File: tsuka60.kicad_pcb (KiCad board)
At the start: 2 copper layers, 285 x 95.1 mm, 175 parts, among them SW1 SW_Push, U1 ATmega32U4-AU, Y1 Resonator_Small

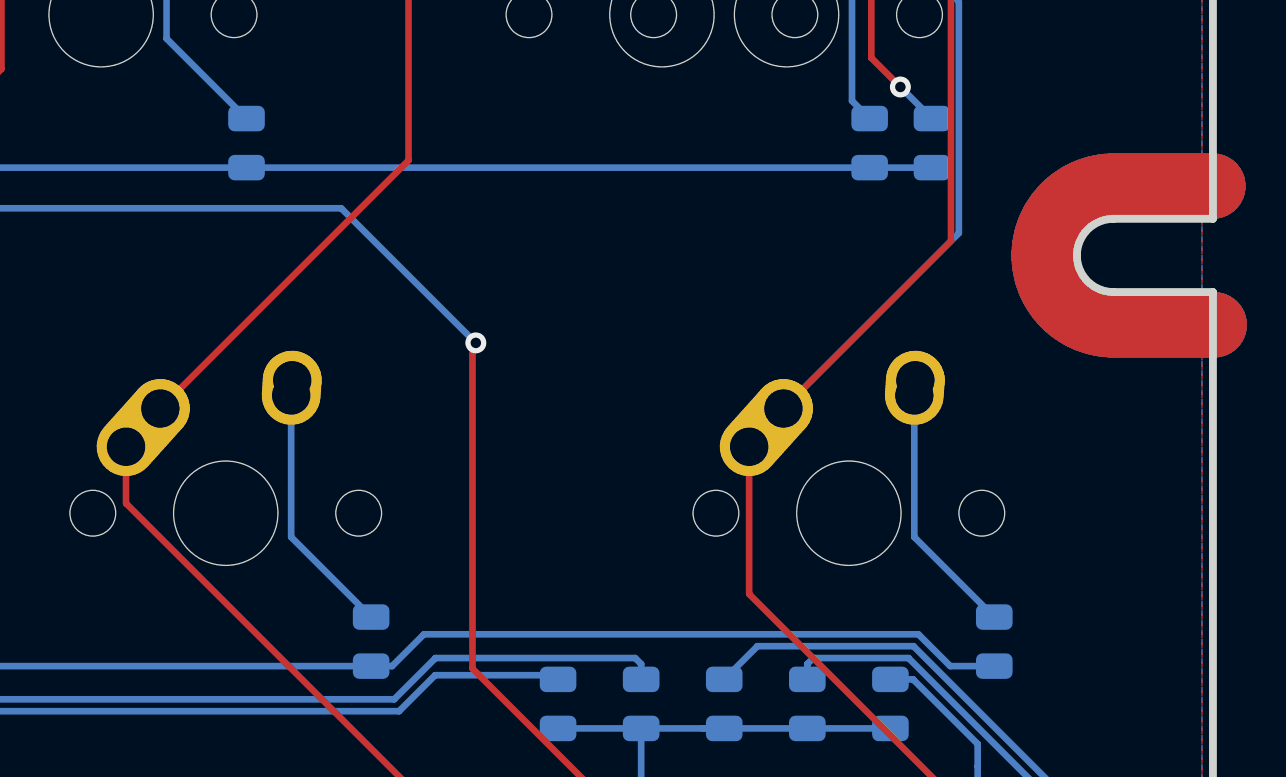
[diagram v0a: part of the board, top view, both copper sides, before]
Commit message: Added alternative right-shift keys
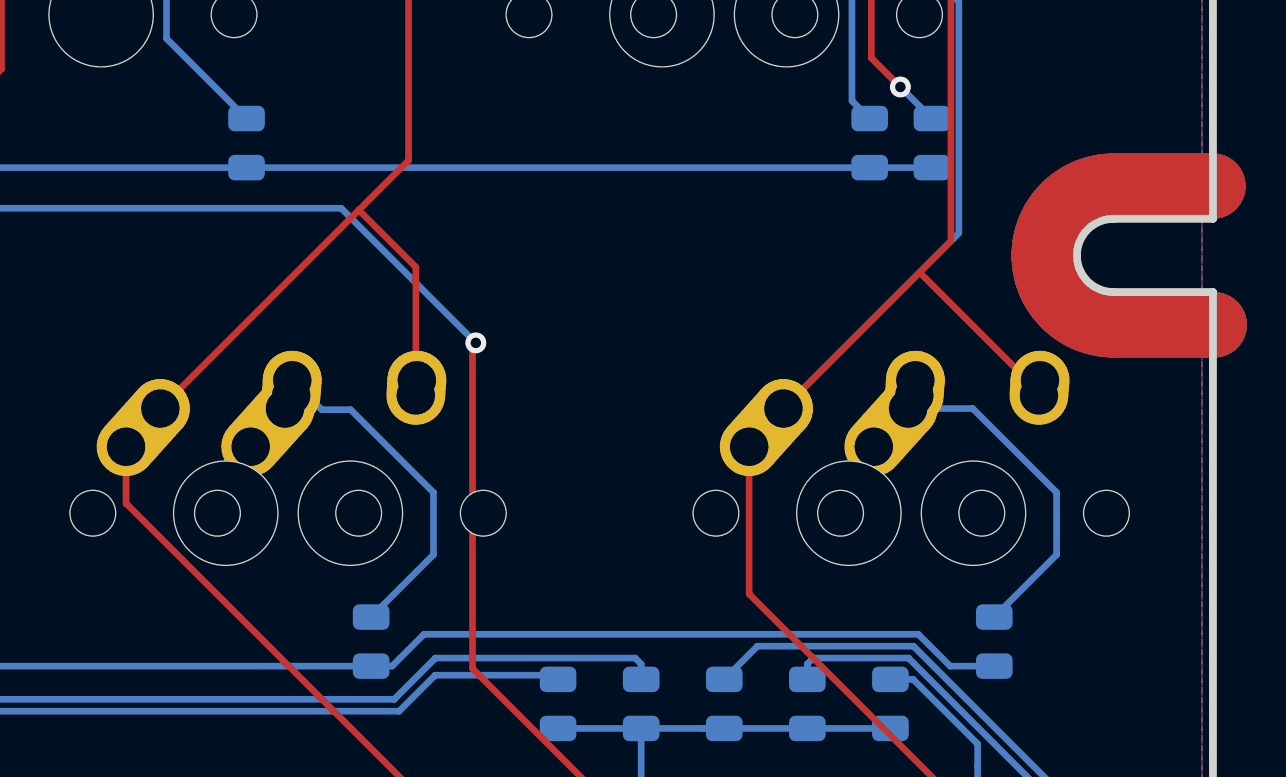
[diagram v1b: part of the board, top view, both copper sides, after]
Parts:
- added MX59-1: SLASH, MX_Alps_Hybrid:MX-1.5U-NoLED, F.Cu at (346.9, 178.6)
- added MX60-1: R-SHIFT, MX_Alps_Hybrid:MX-1U-NoLED, F.Cu at (370.7, 178.6)
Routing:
- net Col13: track 361.5 -> 369.5 mm
- net Col14: track 385.4 -> 392.0 mm
- net Net-(D59-Pad2): track 9.73 -> 12.9 mm
- net Net-(D60-Pad2): track 9.73 -> 12.8 mm
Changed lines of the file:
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@@
     (thickness 1.6)
     (drawings 1)
-    (tracks 1058)
+    (tracks 1069)
     (zones 0)
-    (modules 175)
+    (modules 177)
     (nets 114)
   )
@@
     (38 B.Mask user hide)
     (39 F.Mask user hide)
-    (40 Dwgs.User user hide)
+    (40 Dwgs.User user)
     (41 Cmts.User user hide)
     (42 Eco1.User user hide)
@@
     )
   )
+  (module MX_Alps_Hybrid:MX-1.5U-NoLED (layer F.Cu)
+    (at 346.86875 178.59375)
+    (fp_text reference MX59-1 (at 0 3.175) (layer Dwgs.User)
+      (effects (font (size 1 1) (thickness 0.15)))
+    )
+    (fp_text value SLASH (at 0 -7.9375) (layer Dwgs.User)
+      (effects (font (size 1 1) (thickness 0.15)))
+    )
+    (fp_line (start 5 -7) (end 7 -7) (layer Dwgs.User) (width 0.15))
+    (fp_line (start 7 -7) (end 7 -5) (layer Dwgs.User) (width 0.15))
+    (fp_line (start 5 7) (end 7 7) (layer Dwgs.User) (width 0.15))
+    (fp_line (start 7 7) (end 7 5) (layer Dwgs.User) (width 0.15))
+    (fp_line (start -7 5) (end -7 7) (layer Dwgs.User) (width 0.15))
+    (fp_line (start -7 7) (end -5 7) (layer Dwgs.User) (width 0.15))
+    (fp_line (start -5 -7) (end -7 -7) (layer Dwgs.User) (width 0.15))
+    (fp_line (start -7 -7) (end -7 -5) (layer Dwgs.User) (width 0.15))
+    (fp_line (start -14.2875 -9.525) (end 14.2875 -9.525) (layer Dwgs.User) (width 0.15))
+    (fp_line (start 14.2875 -9.525) (end 14.2875 9.525) (layer Dwgs.User) (width 0.15))
+    (fp_line (start 14.2875 9.525) (end -14.2875 9.525) (layer Dwgs.User) (width 0.15))
+    (fp_line (start -14.2875 9.525) (end -14.2875 -9.525) (layer Dwgs.User) (width 0.15))
+    (pad 2 thru_hole oval (at 2.5 -4.5 86.0548) (size 2.831378 2.25) (drill 1.47 (offset 0.290689 0)) (layers *.Cu B.Mask)
+      (net 92 Col13))
+    (pad 2 thru_hole circle (at 2.54 -5.08) (size 2.25 2.25) (drill 1.47) (layers *.Cu B.Mask)
+      (net 92 Col13))
+    (pad 1 thru_hole oval (at -3.81 -2.54 48.0996) (size 4.211556 2.25) (drill 1.47 (offset 0.980778 0)) (layers *.Cu B.Mask)
+      (net 62 "Net-(D59-Pad2)"))
+    (pad "" np_thru_hole circle (at 0 0) (size 3.9878 3.9878) (drill 3.9878) (layers *.Cu *.Mask))
+    (pad 1 thru_hole circle (at -2.5 -4) (size 2.25 2.25) (drill 1.47) (layers *.Cu B.Mask)
+      (net 62 "Net-(D59-Pad2)"))
+    (pad "" np_thru_hole circle (at -5.08 0 48.0996) (size 1.75 1.75) (drill 1.75) (layers *.Cu *.Mask))
+    (pad "" np_thru_hole circle (at 5.08 0 48.0996) (size 1.75 1.75) (drill 1.75) (layers *.Cu *.Mask))
+  )
+  (module MX_Alps_Hybrid:MX-1U-NoLED (layer F.Cu)
+    (at 370.68125 178.59375)
+    (fp_text reference MX60-1 (at 0 3.175) (layer Dwgs.User)
+      (effects (font (size 1 1) (thickness 0.15)))
+    )
+    (fp_text value R-SHIFT (at 0 -7.9375) (layer Dwgs.User)
+      (effects (font (size 1 1) (thickness 0.15)))
+    )
+    (fp_line (start 5 -7) (end 7 -7) (layer Dwgs.User) (width 0.15))
+    (fp_line (start 7 -7) (end 7 -5) (layer Dwgs.User) (width 0.15))
+    (fp_line (start 5 7) (end 7 7) (layer Dwgs.User) (width 0.15))
+    (fp_line (start 7 7) (end 7 5) (layer Dwgs.User) (width 0.15))
+    (fp_line (start -7 5) (end -7 7) (layer Dwgs.User) (width 0.15))
+    (fp_line (start -7 7) (end -5 7) (layer Dwgs.User) (width 0.15))
+    (fp_line (start -5 -7) (end -7 -7) (layer Dwgs.User) (width 0.15))
+    (fp_line (start -7 -7) (end -7 -5) (layer Dwgs.User) (width 0.15))
+    (fp_line (start -9.525 -9.525) (end 9.525 -9.525) (layer Dwgs.User) (width 0.15))
+    (fp_line (start 9.525 -9.525) (end 9.525 9.525) (layer Dwgs.User) (width 0.15))
+    (fp_line (start 9.525 9.525) (end -9.525 9.525) (layer Dwgs.User) (width 0.15))
+    (fp_line (start -9.525 9.525) (end -9.525 -9.525) (layer Dwgs.User) (width 0.15))
+    (pad 2 thru_hole oval (at 2.5 -4.5 86.0548) (size 2.831378 2.25) (drill 1.47 (offset 0.290689 0)) (layers *.Cu B.Mask)
+      (net 93 Col14))
+    (pad 2 thru_hole circle (at 2.54 -5.08) (size 2.25 2.25) (drill 1.47) (layers *.Cu B.Mask)
+      (net 93 Col14))
+    (pad 1 thru_hole oval (at -3.81 -2.54 48.0996) (size 4.211556 2.25) (drill 1.47 (offset 0.980778 0)) (layers *.Cu B.Mask)
+      (net 63 "Net-(D60-Pad2)"))
+    (pad "" np_thru_hole circle (at 0 0) (size 3.9878 3.9878) (drill 3.9878) (layers *.Cu *.Mask))
+    (pad 1 thru_hole circle (at -2.5 -4) (size 2.25 2.25) (drill 1.47) (layers *.Cu B.Mask)
+      (net 63 "Net-(D60-Pad2)"))
+    (pad "" np_thru_hole circle (at -5.08 0 48.0996) (size 1.75 1.75) (drill 1.75) (layers *.Cu *.Mask))
+    (pad "" np_thru_hole circle (at 5.08 0 48.0996) (size 1.75 1.75) (drill 1.75) (layers *.Cu *.Mask))
+  )
   (gr_text "Tsuka60 aka Semi Ergo Layout\nPrototype Two\nby RominRonin" (at 127.762 131.064) (layer B.SilkS)
     (effects (font (size 1.016 1.016) (thickness 0.254)) (justify right mirror))
@@
   (segment (start 325.55625 179.50625) (end 328.6125 182.5625) (width 0.254) (layer B.Cu) (net 61))
   (segment (start 325.55625 174.09375) (end 325.55625 179.50625) (width 0.254) (layer B.Cu) (net 61))
-  (segment (start 344.60625 179.50625) (end 347.6625 182.5625) (width 0.254) (layer B.Cu) (net 62))
-  (segment (start 344.60625 174.09375) (end 344.60625 179.50625) (width 0.254) (layer B.Cu) (net 62))
-  (segment (start 368.41875 179.50625) (end 371.475 182.5625) (width 0.254) (layer B.Cu) (net 63))
-  (segment (start 368.41875 174.09375) (end 368.41875 179.50625) (width 0.254) (layer B.Cu) (net 63))
+  (segment (start 347.6625 182.5625) (end 350.04375 180.18125) (width 0.254) (layer B.Cu) (net 62))
+  (segment (start 350.04375 180.18125) (end 350.04375 177.8) (width 0.254) (layer B.Cu) (net 62))
+  (segment (start 345.771249 174.638749) (end 344.64625 173.51375) (width 0.254) (layer B.Cu) (net 62))
+  (segment (start 346.882499 174.638749) (end 345.771249 174.638749) (width 0.254) (layer B.Cu) (net 62))
+  (segment (start 350.04375 177.8) (end 346.882499 174.638749) (width 0.254) (layer B.Cu) (net 62))
+  (segment (start 370.65 174.59375) (end 368.18125 174.59375) (width 0.254) (layer B.Cu) (net 63))
+  (segment (start 373.85625 180.18125) (end 373.85625 177.8) (width 0.254) (layer B.Cu) (net 63))
+  (segment (start 373.85625 177.8) (end 370.65 174.59375) (width 0.254) (layer B.Cu) (net 63))
+  (segment (start 371.475 182.5625) (end 373.85625 180.18125) (width 0.254) (layer B.Cu) (net 63))
   (segment (start 138.9125 203.4875) (end 161.925 203.4875) (width 0.254) (layer B.Cu) (net 64))
   (segment (start 138.1125 203.4875) (end 138.9125 203.4875) (width 0.254) (layer B.Cu) (net 64))
@@
   (segment (start 349.09125 144.812712) (end 358.742288 154.46375) (width 0.254) (layer F.Cu) (net 92))
   (segment (start 349.09125 144.30375) (end 349.09125 144.812712) (width 0.254) (layer F.Cu) (net 92))
-  (segment (start 349.09125 165.10875) (end 339.60625 174.59375) (width 0.254) (layer F.Cu) (net 92))
-  (segment (start 349.09125 144.30375) (end 349.09125 165.10875) (width 0.254) (layer F.Cu) (net 92))
   (segment (start 347.82125 118.90375) (end 347.82125 123.22175) (width 0.254) (layer F.Cu) (net 92))
   (segment (start 345.099249 140.311749) (end 349.09125 144.30375) (width 0.254) (layer F.Cu) (net 92))
@@
   (segment (start 156.462518 147.90101) (end 360.62601 147.90101) (width 0.254) (layer B.Cu) (net 92))
   (segment (start 126.223 170.383) (end 133.980528 170.383) (width 0.254) (layer B.Cu) (net 92))
+  (segment (start 349.09125 144.30375) (end 349.09125 165.10875) (width 0.254) (layer F.Cu) (net 92))
+  (segment (start 349.36875 174.09375) (end 349.36875 169.1875) (width 0.254) (layer F.Cu) (net 92))
+  (segment (start 347.190625 167.009375) (end 339.60625 174.59375) (width 0.254) (layer F.Cu) (net 92))
+  (segment (start 349.36875 169.1875) (end 347.190625 167.009375) (width 0.254) (layer F.Cu) (net 92))
+  (segment (start 349.09125 165.10875) (end 347.190625 167.009375) (width 0.254) (layer F.Cu) (net 92))
   (segment (start 361.338251 114.911749) (end 365.649249 114.911749) (width 0.254) (layer B.Cu) (net 93))
   (segment (start 367.056251 116.318751) (end 368.18125 117.44375) (width 0.254) (layer B.Cu) (net 93))
@@
   (segment (start 362.10875 176.05375) (end 362.10875 181.683538) (width 0.254) (layer F.Cu) (net 93))
   (segment (start 364.543749 173.468751) (end 363.41875 174.59375) (width 0.254) (layer F.Cu) (net 93))
-  (segment (start 369.819501 168.192999) (end 364.543749 173.468751) (width 0.254) (layer F.Cu) (net 93))
   (segment (start 369.819501 143.066935) (end 369.819501 168.192999) (width 0.254) (layer F.Cu) (net 93))
   (segment (start 366.87125 140.118684) (end 369.819501 143.066935) (width 0.254) (layer F.Cu) (net 93))
@@
   (segment (start 134.138462 169.583) (end 156.274462 147.447) (width 0.254) (layer B.Cu) (net 93))
   (segment (start 361.76901 148.401943) (end 361.76901 150.179944) (width 0.254) (layer B.Cu) (net 93))
+  (segment (start 373.18125 174.09375) (end 373.18125 173.95) (width 0.254) (layer F.Cu) (net 93))
+  (segment (start 373.18125 173.95) (end 368.621875 169.390625) (width 0.254) (layer F.Cu) (net 93))
+  (segment (start 368.621875 169.390625) (end 364.543749 173.468751) (width 0.254) (layer F.Cu) (net 93))
+  (segment (start 369.819501 168.192999) (end 368.621875 169.390625) (width 0.254) (layer F.Cu) (net 93))
   (segment (start 127.036602 165.583) (end 126.223 165.583) (width 0.254) (layer B.Cu) (net 94))
   (segment (start 127.300001 165.319601) (end 127.036602 165.583) (width 0.254) (layer B.Cu) (net 94))

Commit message: updated the PCB to better accommodate ALPS switches
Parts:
- moved D17 2.38 mm to (128.6, 145.4)
- turned MX17 to 0 degrees
- turned MX29 to 0 degrees
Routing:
- net Net-(D29-Pad2): track 23.8 -> 10.3 mm
- net Net-(D17-Pad2): track 4.05 -> 9.80 mm
- net Col13: track 369.5 -> 367.6 mm
- net Col1: track 110.4 -> 112.1 mm
- net Row1: track 293.7 -> 294.8 mm
- net GND: vias 30 -> 32
